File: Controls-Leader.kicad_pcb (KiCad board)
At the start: 2 copper layers, 99.5 x 94.2 mm, 164 parts, among them J1 Left_Signal, J10 Conn_02x03_Top_Bottom, J11 Conn_02x03_Top_Bottom, J12 Conn_01x04, J13 Conn_01x04, J18 PowerConn, J2 Right_Signal, J20 MotorCANConnector, J21 CAN_IN, J22 CAN_OUT, J23 USB_B_Micro, J24 ExtraGPIO_Conn, J25 UART_TP, J26 CAN_TP, J27 CAN_TP, J28 KILL_SW_IND, J29 Headlight, J3 Brake Light, J30 Backup Camera, J4 Headlight, J5 MinionConn, J6 SPI, J7 BPS_PWR_OUT, J8 SWD, J9 POW_2ND_CONN, SW1 BACKUP_SW, SW10 RESET, SW8 SW_Rotary2x6, U1 EL3H7, U10 EL3H7, U11 EL3H7, U12 RI3-1205S, U13 NCP1117-3.3_SOT223, U14 ADM3055E, U15 CDSOT23-T24CAN, U17 ADM3055E, U18 CDSOT23-T24CAN, U19 CP2102N-A01-GQFN24, U2 EL3H7, U3 EL3H7, U4 EL3H7, U5 EL3H7, U6 EL3H7, U7 STM32F413RHTx, U8 EL3H7, U9 EL3H7, Y1 Crystal

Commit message: layout in progress
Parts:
- removed C18, C19: 0.1uF, Capacitor_SMD:C_0805_2012Metric
- removed C2, C3, C32: 1u, Capacitor_SMD:C_0805_2012Metric
- removed C20: 10u, UTSVT_Passive:C_2220_5750Metric
- removed D1: KILL_SW_LED, UTSVT_Connectors:Molex_MicroFit3.0_1x2xP3.00mm_PolarizingPeg_Vertical
- removed D4, D5: BAS70-04, Package_TO_SOT_SMD:SOT-23
- removed D6: TVS, Diode_SMD:D_SOD-323
- removed J13: Conn_01x04, Connector_Molex:Molex_Micro-Fit_3.0_43650-0415_1x04_P3.00mm_Vertical
- removed J20: MotorCANConnector, UTSVT_Connectors:TE_4-2172079-2
- removed J28: KILL_SW_IND, UTSVT_Connectors:Molex_MicroFit3.0_1x2xP3.00mm_PolarizingPeg_Vertical
- removed J29: Headlight, UTSVT_Connectors:Molex_MicroFit3.0_1x2xP3.00mm_PolarizingPeg_Vertical
- removed J30: Backup Camera, Connector_Molex:Molex_Micro-Fit_3.0_43650-0215_1x02_P3.00mm_Vertical
- removed JP3, JP4: Jumper_2_Bridged, Jumper:SolderJumper-2_P1.3mm_Open_Pad1.0x1.5mm
- removed L1, L2, L3, L4, L9: 22u, Inductor_SMD:L_0805_2012Metric
- removed PS1, PS2, PS3, PS4, PS5: RCD-24, UTSVT_Special:RCD-24
- removed SW1: BACKUP_SW, Connector_Molex:Molex_Micro-Fit_3.0_43650-0315_1x03_P3.00mm_Vertical
- removed SW8: SW_Rotary2x6, Connector_Molex:Molex_Micro-Fit_3.0_43045-1412_2x07_P3.00mm_Vertical
- removed TP1: LEFT_BLINK, TestPoint:TestPoint_Pad_D1.5mm
- removed TP13: +12VA_TP, TestPoint:TestPoint_Pad_1.5x1.5mm
- removed TP14: GND1_TP, TestPoint:TestPoint_Pad_1.5x1.5mm
- removed TP2: +12V_TP, TestPoint:TestPoint_Pad_1.5x1.5mm
- removed TP3: GNDPWR_TP, TestPoint:TestPoint_Pad_1.5x1.5mm
- removed U10, U11: EL3H7, Package_SO:SOP-4_4.4x2.6mm_P1.27mm
- added BRAKELIGHT1: EXTERNAL_BRAKELIGHT, Connector_Molex:Molex_Micro-Fit_3.0_43650-0215_1x02_P3.00mm_Vertical, F.Cu at (125.5, 168.3)
- added D10: Motor Controller Fault, LED_SMD:LED_0805_2012Metric, F.Cu at (30.0, 37.3)
- added D11: Ignition 1, LED_SMD:LED_0805_2012Metric, F.Cu at (30.0, 40.3)
- added D12: Ignition 2, LED_SMD:LED_0805_2012Metric, F.Cu at (30.0, 43.4)
- added D13: BPS Fault, LED_SMD:LED_0805_2012Metric, F.Cu at (30.0, 46.4)
- added D16: Control Fault, LED_SMD:LED_0805_2012Metric, F.Cu at (30.0, 49.5)
- added D17: SD12_SOD323, Diode_SMD:D_SOD-323, F.Cu at (110.3, 7.05)
- added D18: A_CNCTR, LED_SMD:LED_0805_2012Metric, F.Cu at (30.0, 52.5)
- added D7: M_CNCTR, LED_SMD:LED_0805_2012Metric, F.Cu at (30.0, 31.2)
- added D9: OS Error, LED_SMD:LED_0805_2012Metric, F.Cu at (30.0, 34.3)
- added F1: Fuse, Fuse:Fuse_1206_3216Metric, F.Cu at (109.4, 57.3)
- added J14: Conn_02x04_Odd_Even, UTSVT_Connectors:Molex_MicroFit3.0_2x4xP3.00mm_PolarizingPeg_Vertical, F.Cu at (221.0, 82.2)
- added LOGO3: Dr. Hallock Logo, UTSVT_Special:Hallock_Image_Small, F.Cu at (7.62, -15.2)
- added LOGO4: UTSVT Logo, UTSVT_Special:UTSVT_Logo_Symbol, F.Cu at (-5.08, 7.62)
- added L_BLINK_EXT1: EXTERNAL_LEFTBLINK, Connector_Molex:Molex_Micro-Fit_3.0_43650-0215_1x02_P3.00mm_Vertical, F.Cu at (112.2, 168.3)
- added Q1: IRLML0030, Package_TO_SOT_SMD:SOT-23, F.Cu at (113.8, 161.0)
- added Q2: IRLML0030, Package_TO_SOT_SMD:SOT-23, F.Cu at (111.3, 21.7)
- added Q3: IRLML0030, Package_TO_SOT_SMD:SOT-23, F.Cu at (100.3, 161.0)
- added Q4: IRLML0030, Package_TO_SOT_SMD:SOT-23, F.Cu at (85.8, 79.1)
- added Q5: IRLML0030, Package_TO_SOT_SMD:SOT-23, F.Cu at (30.4, 79.7)
- added Q6: IRLML0030, Package_TO_SOT_SMD:SOT-23, F.Cu at (30.4, 84.4)
- added R28: 698, Resistor_SMD:R_0805_2012Metric, F.Cu at (19.4, 44.4)
- added R31: 698, Resistor_SMD:R_0805_2012Metric, F.Cu at (19.4, 47.3)
- added R33: 4.9k, Resistor_SMD:R_0805_2012Metric, F.Cu at (17.0, 78.8)
- added R39: 2k, Resistor_SMD:R_0805_2012Metric, F.Cu at (17.0, 81.8)
- added R41: 100k, Resistor_SMD:R_0805_2012Metric, F.Cu at (81.1, 77.8)
- added R50: 4.9k, Resistor_SMD:R_0805_2012Metric, F.Cu at (17.0, 84.7)
- added R52: 2k, Resistor_SMD:R_0805_2012Metric, F.Cu at (17.0, 87.7)
- added R53: 4.9k, Resistor_SMD:R_0805_2012Metric, F.Cu at (21.4, 78.8)
- added R55: 2k, Resistor_SMD:R_0805_2012Metric, F.Cu at (21.4, 81.8)
- added R56: 100k, Resistor_SMD:R_0805_2012Metric, F.Cu at (81.1, 80.7)
- added R58: 100k, Resistor_SMD:R_0805_2012Metric, F.Cu at (81.1, 83.7)
- added R59: 4.9k, Resistor_SMD:R_0805_2012Metric, F.Cu at (21.4, 84.7)
- added R60: 2k, Resistor_SMD:R_0805_2012Metric, F.Cu at (21.4, 87.7)
- added R61: 4.9k, Resistor_SMD:R_0805_2012Metric, F.Cu at (25.8, 78.8)
- added R62: 2k, Resistor_SMD:R_0805_2012Metric, F.Cu at (25.8, 81.8)
- added R63: 4.9k, Resistor_SMD:R_0805_2012Metric, F.Cu at (25.8, 84.7)
- added R64: 2k, Resistor_SMD:R_0805_2012Metric, F.Cu at (25.8, 87.7)
- added R8: 698, Resistor_SMD:R_0805_2012Metric, F.Cu at (15.0, 44.4)
- added R9: 698, Resistor_SMD:R_0805_2012Metric, F.Cu at (15.0, 47.3)
- added R_BLINK_EXT1: EXTERNAL_RIGHTBLINK, Connector_Molex:Molex_Micro-Fit_3.0_43650-0215_1x02_P3.00mm_Vertical, F.Cu at (98.6, 168.3)
- added U23: EL3H7, Package_DIP:DIP-4_W7.62mm, F.Cu at (1.12, 80.9)
- added U24: EL3H7, Package_DIP:DIP-4_W7.62mm, F.Cu at (1.12, 87.6)
- added U25: EL3H7, Package_DIP:DIP-4_W7.62mm, F.Cu at (69.7, 76.2)
- added U26: EL3H7, Package_DIP:DIP-4_W7.62mm, F.Cu at (101.6, 148.6)
- added U27: EL3H7, Package_DIP:DIP-4_W7.62mm, F.Cu at (1.12, 94.3)
- added U28: EL3H7, Package_DIP:DIP-4_W7.62mm, F.Cu at (1.12, 101.0)
- added U29: EL3H7, Package_DIP:DIP-4_W7.62mm, F.Cu at (16.5, 116.8)
- C1: value 1u -> 1uF
- C14, C15, C28, C38, C41, LOGO1: moved to F.Cu
- C4: value 1u -> 10u
- J1: value Left_Signal -> Conn_01x02; footprint UTSVT_Connectors:Molex_MicroFit3.0_1x2xP3.00mm_PolarizingPeg_Vertical -> Connector_Molex:Molex_Micro-Fit_3.0_43650-0215_1x02_P3.00mm_Vertical
- J10, J11: value Conn_02x03_Top_Bottom -> Conn_01x02; footprint Connector_Molex:Molex_Micro-Fit_3.0_43045-0612_2x03_P3.00mm_Vertical -> Connector_Molex:Molex_Micro-Fit_3.0_43650-0215_1x02_P3.00mm_Vertical
- J12: value Conn_01x04 -> Conn_01x02; footprint Connector_Molex:Molex_Micro-Fit_3.0_43650-0415_1x04_P3.00mm_Vertical -> Connector_Molex:Molex_Micro-Fit_3.0_43650-0215_1x02_P3.00mm_Vertical
- J2: value Right_Signal -> UART_TP; footprint UTSVT_Connectors:Molex_MicroFit3.0_1x2xP3.00mm_PolarizingPeg_Vertical -> Connector_PinHeader_2.54mm:PinHeader_1x03_P2.54mm_Vertical
- J3: value Brake Light -> ExtraGPIO_Conn; footprint UTSVT_Connectors:Molex_MicroFit3.0_1x2xP3.00mm_PolarizingPeg_Vertical -> Connector_PinHeader_2.54mm:PinHeader_2x05_P2.54mm_Vertical
- J4: value Headlight -> Conn_02x05_Top_Bottom; footprint UTSVT_Connectors:Molex_MicroFit3.0_1x2xP3.00mm_PolarizingPeg_Vertical -> UTSVT_Connectors:Molex_MicroFit3.0_2x6xP3.00mm_PolarizingPeg_Vertical
- J5: value MinionConn -> M_CAN_IN; footprint Connector_Molex:Molex_Micro-Fit_3.0_43045-1012_2x05_P3.00mm_Vertical -> Connector_Molex:Molex_Micro-Fit_3.0_43045-0612_2x03_P3.00mm_Vertical
- J6: value SPI -> Conn_01x04; footprint Connector_PinHeader_2.54mm:PinHeader_1x04_P2.54mm_Vertical -> Connector_Molex:Molex_Micro-Fit_3.0_43650-0415_1x04_P3.00mm_Vertical
- J7: value BPS_PWR_OUT -> Conn_01x03; footprint UTSVT_Connectors:Molex_MicroFit3.0_1x2xP3.00mm_PolarizingPeg_Vertical -> Connector_Molex:Molex_Micro-Fit_3.0_43650-0315_1x03_P3.00mm_Vertical
- J9: value POW_2ND_CONN -> Conn_01x03; footprint UTSVT_Connectors:Molex_MicroFit3.0_1x2xP3.00mm_PolarizingPeg_Vertical -> Connector_Molex:Molex_Micro-Fit_3.0_43650-0315_1x03_P3.00mm_Vertical
- L5, L6, L7, L8: value 2kH -> https://www.mouser.com/ProductDetail/963-BK2125LM182-T
- R1, R2, R3, R4: value 105 -> 698
- R10: value 4.9k -> 2k
- R11: value 4.9k -> 510
- R12: value 1.2k -> 510
- R19: value 5.1k -> 510
- R20: value 5.1k -> 100k
- R22: value 10k -> 510
- R23: value 10k -> 100k
- R26, R27: value 105R -> 10k
- R5: value 510 -> 2k
- R7: value 1.5k -> 5.1k
- TP10: value POWER -> GND_UNISO; footprint TestPoint:TestPoint_Pad_1.5x1.5mm -> TestPoint:TestPoint_Keystone_5005-5009_Compact
- TP7: footprint TestPoint:TestPoint_Pad_D1.5mm -> TestPoint:TestPoint_Pad_1.5x1.5mm
- TP8: value BK_LIGHT -> LEFT_BLINK; footprint TestPoint:TestPoint_Pad_D1.5mm -> TestPoint:TestPoint_Pad_1.5x1.5mm
- TP9: value Headlight_PWR -> 12V_UNISO; footprint TestPoint:TestPoint_Pad_D1.5mm -> TestPoint:TestPoint_Keystone_5005-5009_Compact
- U1, U2, U3, U4, U5, U6, U8, U9: footprint Package_SO:SOP-4_4.4x2.6mm_P1.27mm -> Package_DIP:DIP-4_W7.62mm
- moved LOGO1 166.5 mm to (-40.6, 22.9), turned to 0 degrees
- moved U4 165.6 mm to (1.12, 67.5), turned to 0 degrees
- moved H4 163.7 mm to (53.3, 170.2), turned to 0 degrees
- moved U2 160.6 mm to (1.12, 60.8), turned to 0 degrees
- moved R4 158.1 mm to (15.0, 41.4), turned to 0 degrees
- moved R3 152.4 mm to (10.6, 47.3), turned to 0 degrees
- moved R2 150.6 mm to (10.6, 44.4), turned to 0 degrees
- moved U5 150.0 mm to (1.12, 74.2), turned to 0 degrees
- moved J22 149.8 mm to (244.4, 124.0), turned to 0 degrees
- moved R1 149.3 mm to (10.6, 41.4), turned to 0 degrees
- moved J1 147.8 mm to (43.7, 44.0), turned to 0 degrees
- moved J21 147.4 mm to (244.4, 116.8), turned to 0 degrees
- moved H3 136.6 mm to (228.6, 172.7)
- moved LOGO2 133.4 mm to (-5.08, 15.2)
- moved U12 131.0 mm to (97.2, 6.60), turned to 0 degrees
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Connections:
- C1 pad 1: GNDPWR -> /Brake_SW
- C1 pad 2: +12V -> GND
- C4 pad 1: GNDPWR -> +12V
- C4 pad 2: +12V -> Net-(Q2-D)
- J1 pad 1: Net-(J1-Pad1) -> /ADC1_IN8
- J1 pad 2: Net-(J1-Pad2) -> /ADC1_IN9
- J10 pad 1: +3V3 -> Net-(J10-Pin_1)
- J10 pad 2: Net-(R15-Pad1) -> Net-(J10-Pin_2)
- J11 pad 1: +3V3 -> Net-(J11-Pin_1)
- J11 pad 2: Net-(R16-Pad1) -> Net-(J11-Pin_2)
- J12 pad 1: Net-(U9-Pad4) -> +3.3V
- J12 pad 2: Net-(U9-Pad3) -> Net-(J12-Pin_2)
- J2 pad 1: Net-(J2-Pad1) -> GND
- J2 pad 2: Net-(J2-Pad2) -> /UART4_Tx
- J24 pad 2: /PB4 -> /PB2
- J24 pad 4: /PB5 -> /PB3
- J24 pad 6: /PB6 -> /PD2
- J24 pad 8: /PB7 -> /PC12
- J3 pad 1: Net-(J3-Pad1) -> /PC8
- J3 pad 2: Net-(J3-Pad2) -> /PC2
- J4 pad 1: Net-(J4-Pad1) -> +12V
- J4 pad 2: Net-(J4-Pad2) -> /DashAndDisplay/BPS_Hzd
- J5 pad 1: +5V -> Net-(J5-Pin_1)
- J5 pad 3: /MOSI -> unconnected-(J5-Pin_3-Pad3)
- J5 pad 4: /MISO -> /Motor_CAN/CAN_H
- J5 pad 5: /BPS_PWR -> /Motor_CAN/CAN_L
- J5 pad 6: /UART3_Tx -> unconnected-(J5-Pin_6-Pad6)
- J6 pad 1: /MOSI -> +5V
- J6 pad 2: /MISO -> GND
- J6 pad 3: /CLK -> /UART3_Tx
- J6 pad 4: /CS -> /UART3_Rx
- J7 pad 1: /BPS_PWR -> +3V3
- J7 pad 2: GNDPWR -> Net-(J7-Pin_2)
- J9 pad 1: Net-(J9-Pad1) -> +3V3
- J9 pad 2: GNDPWR -> Net-(J9-Pin_2)
- R1 pad 1: Net-(R1-Pad1) -> /Motor_PRCHG_Bypass
- R1 pad 2: /LEFT_BLINK -> Net-(D7-A)
- R10 pad 1: +3V3 -> Net-(R10-Pad1)
- R10 pad 2: /IG1 -> /Left_Ind
- R11 pad 1: +3V3 -> /Lights/RIGHT_BLINK
- R11 pad 2: /IG2 -> Net-(R11-Pad2)
- R12 pad 1: Net-(J28-Pad1) -> /Lights/LEFT_BLINK
- R15 pad 1: Net-(R15-Pad1) -> Net-(J7-Pin_2)
- R16 pad 1: Net-(R16-Pad1) -> Net-(J9-Pin_2)
- R19 pad 1: +3V3 -> /Heartbeat
- R19 pad 2: /Brake_Pot2 -> Net-(R19-Pad2)
- R2 pad 1: Net-(R2-Pad1) -> /OS_Fault
- R2 pad 2: /RIGHT_BLINK -> Net-(D9-A)
- R20 pad 1: /Accel_Pot2 -> Net-(Q5-G)
- R20 pad 2: GND -> GNDPWR
- R22 pad 1: Net-(R22-Pad1) -> /Bps_Hazard
- R22 pad 2: /Accel_Pot2 -> Net-(R22-Pad2)
- R23 pad 1: Net-(R23-Pad1) -> Net-(Q6-G)
- R23 pad 2: /Brake_Pot2 -> GNDPWR
- R24 pad 2: /M_PRCHG -> /Array_PRCHG_Bypass
- R25 pad 2: /M_CNCTR -> /Motor_PRCHG_Bypass
- R26 pad 1: Net-(R26-Pad1) -> Net-(J12-Pin_2)
- R26 pad 2: /A_CNCTR -> GND
- R27 pad 1: Net-(R27-Pad1) -> /Brake_SW
- R27 pad 2: /A_PRCHG -> Net-(J12-Pin_2)
- R3 pad 1: Net-(R3-Pad1) -> /Motor_Controller_Fault
- R3 pad 2: /BK_LIGHT -> Net-(D10-A)
- R4 pad 1: Net-(R4-Pad1) -> /IG1
- R4 pad 2: /Headlight_ON -> Net-(D11-A)
- R5 pad 2: Net-(R5-Pad2) -> /Right_Ind
- R6 pad 1: Net-(R6-Pad1) -> /Brake_Light
- TP10 pad 1: Net-(SW8-Pad11) -> GNDPWR
- TP7 pad 1: /RIGHT_BLINK -> /Lights/RIGHT_BLINK
- TP8 pad 1: /BK_LIGHT -> /Lights/LEFT_BLINK
- TP9 pad 1: /Headlight_ON -> +12V
- U1 pad 1: Net-(R1-Pad1) -> Net-(R10-Pad1)
- U1 pad 2: GND -> GNDPWR
- U1 pad 3: Net-(PS1-Pad3) -> /Lights/LEFT_BLINK
- U1 pad 4: +12V -> /TimerCLK
- U12 pad 1: GNDPWR -> Net-(Q2-D)
- U2 pad 1: Net-(R2-Pad1) -> Net-(R39-Pad2)
- U2 pad 2: GND -> GNDPWR
- U2 pad 3: Net-(PS2-Pad3) -> /IG1
- U2 pad 4: +12V -> +3V3
- U3 pad 1: Net-(R3-Pad1) -> Net-(R6-Pad2)
- U4 pad 1: Net-(R4-Pad1) -> Net-(R19-Pad2)
- U4 pad 3: Net-(PS4-Pad3) -> Net-(Q5-G)
- U5 pad 1: Net-(R5-Pad2) -> Net-(R22-Pad2)
- U5 pad 2: GNDPWR -> GND
- U5 pad 3: GND -> Net-(Q6-G)
- U5 pad 4: /IG1 -> +12V
- U6 pad 1: Net-(R6-Pad2) -> Net-(R5-Pad1)
- U6 pad 3: GND -> /Lights/RIGHT_BLINK
- U6 pad 4: /IG2 -> /TimerCLK
- U7 pad 10: /Accel_Pot2 -> /PC2
- U7 pad 11: /Brake_Pot2 -> /PC3
- U7 pad 20: /CS -> /Bps_Hazard
- U7 pad 21: /CLK -> /Forward
- U7 pad 22: /MISO -> /Reverse
- U7 pad 23: /MOSI -> /Cruise_En
- U7 pad 24: unconnected-(U7-Pad24) -> /PC4
- U7 pad 26: unconnected-(U7-Pad26) -> /ADC1_IN8
- U7 pad 27: unconnected-(U7-Pad27) -> /ADC1_IN9
- U7 pad 28: unconnected-(U7-Pad28) -> /PB2
- U7 pad 33: unconnected-(U7-Pad33) -> /UART4_Rx
- U7 pad 34: unconnected-(U7-Pad34) -> /UART4_Tx
- U7 pad 35: unconnected-(U7-Pad35) -> /BPS_Fault
- U7 pad 36: unconnected-(U7-Pad36) -> /Controls_Fault
- U7 pad 37: /Headlight_ON -> /PC6
- U7 pad 38: /BK_LIGHT -> /PC7
- U7 pad 39: /RIGHT_BLINK -> /PC8
- U7 pad 40: /LEFT_BLINK -> /Brake_SW
- U7 pad 42: unconnected-(U7-Pad42) -> /PA9
- U7 pad 43: unconnected-(U7-Pad43) -> /PA10
- U7 pad 51: /A_PRCHG -> /Array_PRCHG_Bypass
- U7 pad 52: /A_CNCTR -> /Motor_PRCHG_Bypass
- U7 pad 53: /M_CNCTR -> /PC12
- U7 pad 54: /M_PRCHG -> /PD2
- U7 pad 55: unconnected-(U7-Pad55) -> /PB3
- U7 pad 56: /PB4 -> /Cruise_Set
- U7 pad 57: /PB5 -> /Brake_Light
- U7 pad 58: /PB6 -> /Heartbeat
- U7 pad 59: /PB7 -> /TimerCLK
- U7 pad 61: unconnected-(U7-Pad61) -> /OS_Fault
- U7 pad 62: unconnected-(U7-Pad62) -> /Motor_Controller_Fault
- U8 pad 3: Net-(U8-Pad3) -> Net-(J10-Pin_2)
- U8 pad 4: Net-(U8-Pad4) -> Net-(J10-Pin_1)
- U9 pad 3: Net-(U9-Pad3) -> Net-(J11-Pin_2)
- U9 pad 4: Net-(U9-Pad4) -> Net-(J11-Pin_1)
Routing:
- net +3V3: track 299.6 -> 0.00 mm, vias 18 -> 0
- net +12V: track 190.8 -> 0.00 mm, vias 5 -> 0
- net GNDPWR: track 185.9 -> 0.00 mm, vias 43 -> 0
- net +5V: track 146.2 -> 0.00 mm, vias 6 -> 0
- net GND: track 71.2 -> 0.00 mm, vias 131 -> 0
- net /Accel_Pot: track 66.0 -> 0.00 mm
- net /Accel_Pot2: track 60.7 -> 0.00 mm
- net /Brake_Pot2: track 60.3 -> 0.00 mm, vias 4 -> 0
- net /Car_CAN/CAN_L: track 56.7 -> 0.00 mm, vias 1 -> 0
- net Net-(U15-GND): track 55.4 -> 0.00 mm, vias 4 -> 0
- net Net-(J21-Pin_2): track 54.2 -> 0.00 mm, vias 2 -> 0
- net /LEFT_BLINK: track 54.1 -> 0.00 mm
- net /UART3_Tx: track 53.9 -> 0.00 mm
- net /Car_CAN/CAN_H: track 53.5 -> 0.00 mm
- net /Brake_Pot: track 49.8 -> 0.00 mm, vias 2 -> 0
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- removed copper zone on B.Cu, net GND
- removed copper zone on F.Cu, net GND
- removed copper zone on B.Cu, net GNDPWR
- removed copper zone on F.Cu, net GNDPWR
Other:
- board outline removed
- board text removed: "+"
- board text removed: "+12V"
- board text removed: "+5V"
- board text removed: "-"
- board text removed: "12VA"
- board text removed: "3.3V"
- board text removed: "3V3"
- board text removed: "5V"
- board text removed: "Accel"
- board text removed: "Accel Cntctr"
- board text removed: "BPS Pwr"
- board text removed: "BPSEN"
- board text removed: "Backup Cam"
- board text removed: "Brake"
- board text removed: "CAN"
- board text removed: "CLK"
- board text removed: "CS"
- board text removed: "Camera Switch"
- board text removed: "Controls Leader Board v2.4 Chase Block & Hannah Lee April 2022"
- board text removed: "DIO"
- board text removed: "GND"
- board text removed: "GND1"
- board text removed: "GNDPWR"
- board text removed: "HeadLights"
- board text removed: "Headlight"
- board text removed: "Ign Sw"
- board text removed: "Kill Sw Ctrl"
- board text removed: "Kill Sw LED"
- board text removed: "Left"
- board text removed: "Left Blink"
- board text removed: "MISO"
- board text removed: "MOSI"
- board text removed: "Minion"
- board text removed: "Motor Cntctr"
- board text removed: "Pwr 2nd Conn"
- board text removed: "Right"
- board text removed: "Right Blink"
- board text removed: "Rx"
- board text removed: "TO-DOS: - Fix minion brd connector so that way 12v and gndpwr and 5v and gnd are next to each other respectively. It would also be nice to change it to be a larger connector so we can send +5v and gnd to the minion brd - Finish labelling the connector and test points in the power section - Finish the traces - Rename the board"
- board text removed: "Tx"

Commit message: routing done for optocouplers
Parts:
- moved U6 186.3 mm to (133.5, 186.6), turned to 90 degrees
- moved R5 182.6 mm to (134.1, 189.8), turned to 180 degrees
- moved U1 172.2 mm to (137.7, 163.6)
- moved TP7 169.8 mm to (150.6, 168.9)
- moved TP8 168.1 mm to (154.2, 168.9)
- moved U2 163.9 mm to (116.3, 177.3), turned to 90 degrees
- moved U4 162.6 mm to (137.2, 156.5)
- moved R4 158.6 mm to (117.5, 162.6), turned to 180 degrees
- moved R10 157.3 mm to (134.5, 166.1), turned to -90 degrees
- moved R20 156.0 mm to (148.8, 157.6), turned to -90 degrees
- moved U24 152.9 mm to (125.0, 177.3), turned to 90 degrees
- moved R8 148.5 mm to (105.0, 162.6), turned to 180 degrees
- moved D11 147.4 mm to (117.4, 159.0), turned to 180 degrees
- moved R19 145.2 mm to (134.4, 157.8), turned to -90 degrees
- moved U23 144.5 mm to (108.7, 177.3), turned to 90 degrees
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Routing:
- net Net-(Q5-G): track 0.00 -> 37.1 mm
- net Net-(Q6-G): track 0.00 -> 32.1 mm
- net /Left_Ind: track 0.00 -> 25.7 mm
- net /Lights/RIGHT_BLINK: track 0.00 -> 22.0 mm
- net /DashAndDisplay/IGN_2_Motor: track 0.00 -> 21.2 mm
- net /Lights/LEFT_BLINK: track 0.00 -> 18.4 mm
- net Net-(R11-Pad2): track 0.00 -> 18.2 mm
- net Net-(R62-Pad2): track 0.00 -> 17.0 mm
- net Net-(J10-Pin_1): track 0.00 -> 15.2 mm
- net Net-(J11-Pin_1): track 0.00 -> 15.1 mm
- net Net-(J11-Pin_2): track 0.00 -> 14.8 mm
- net Net-(J10-Pin_2): track 0.00 -> 14.8 mm
- net Net-(R60-Pad2): track 0.00 -> 13.9 mm
- net Net-(R24-Pad1): track 0.00 -> 12.9 mm
- net Net-(R25-Pad1): track 0.00 -> 12.9 mm
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
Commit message: layout done except connecting uc to everything and vias for power and gnd plane
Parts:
- D10: value Motor Controller Fault -> Motor Fault
- moved J6 204.0 mm to (81.7, 58.5), turned to -90 degrees
- moved J1 186.1 mm to (212.8, 122.0), turned to 90 degrees
- moved R3 165.8 mm to (165.0, 107.7)
- moved R9 155.1 mm to (158.9, 105.2)
- moved D10 151.1 mm to (165.0, 105.2), turned to 180 degrees
- moved J14 148.1 mm to (80.7, 129.9)
- moved C4 143.6 mm to (208.7, 101.3), turned to 90 degrees
- moved D13 142.7 mm to (158.8, 107.7)
- moved TP9 142.2 mm to (209.2, 109.3)
- moved R28 141.5 mm to (147.2, 105.2)
- moved U12 141.4 mm to (203.6, 99.7), turned to 90 degrees
- moved R2 139.4 mm to (136.1, 105.2)
- moved C40 137.9 mm to (196.0, 53.2), turned to -90 degrees
- moved R18 136.1 mm to (151.4, 74.8)
- moved C39 135.1 mm to (193.0, 53.2), turned to -90 degrees
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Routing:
- net Net-(J21-Pin_2): track 0.00 -> 86.4 mm
- net /Car_CAN/CAN_H: track 0.00 -> 82.7 mm
- net /UART3_Rx: track 0.00 -> 77.3 mm
- net /Motor_CAN/CAN_H: track 0.00 -> 73.2 mm
- net /UART3_Tx: track 0.00 -> 71.3 mm
- net /Accel_Pot: track 0.00 -> 61.9 mm
- net /Car_CAN/CAN_L: track 0.00 -> 60.7 mm
- net Net-(J21-Pin_1): track 0.00 -> 57.2 mm
- net /Motor_CAN/CAN_L: track 0.00 -> 49.6 mm
- net /Brake_Pot: track 0.00 -> 40.7 mm
- net Net-(U15-GND): track 0.00 -> 27.2 mm
- net /Brake_SW: track 0.00 -> 26.9 mm
- net /NRST: track 0.00 -> 20.6 mm
- net Net-(C37-Pad2): track 0.00 -> 13.7 mm
- net +5V: track 0.00 -> 12.6 mm
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- added copper zone on In1.Cu, net +3.3V
- added copper zone on In2.Cu, net GND
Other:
- board outline added: 137.7 x 115.3 mm
- copper layers 2 -> 4

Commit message: Shuffled some things closer together.
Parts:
- moved J1 45.8 mm to (196.3, 79.2)
- moved C16 23.1 mm to (109.1, 64.5)
- moved C17 23.1 mm to (109.1, 79.8)
- moved D2 23.1 mm to (109.5, 68.5)
- moved R13 23.1 mm to (105.5, 83.9)
- moved R14 23.1 mm to (105.5, 68.5)
- moved R15 23.1 mm to (105.5, 64.5)
- moved R16 23.1 mm to (105.5, 79.8)
- moved R26 23.1 mm to (109.4, 96.1)
- moved C1 23.1 mm to (108.0, 92.5)
- moved D3 23.1 mm to (110.0, 83.9)
- moved J12 23.1 mm to (99.9, 94.0)
- moved J14 23.1 mm to (98.9, 115.8)
- moved J6 23.1 mm to (99.9, 44.4)
- moved J7 23.1 mm to (99.9, 62.5)
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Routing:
- net GND: track 0.00 -> 13.2 mm
- net Net-(J11-Pin_2): track 14.8 -> 1.59 mm
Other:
- board size 137.7 x 115.3 mm -> 137.7 x 115.6 mm

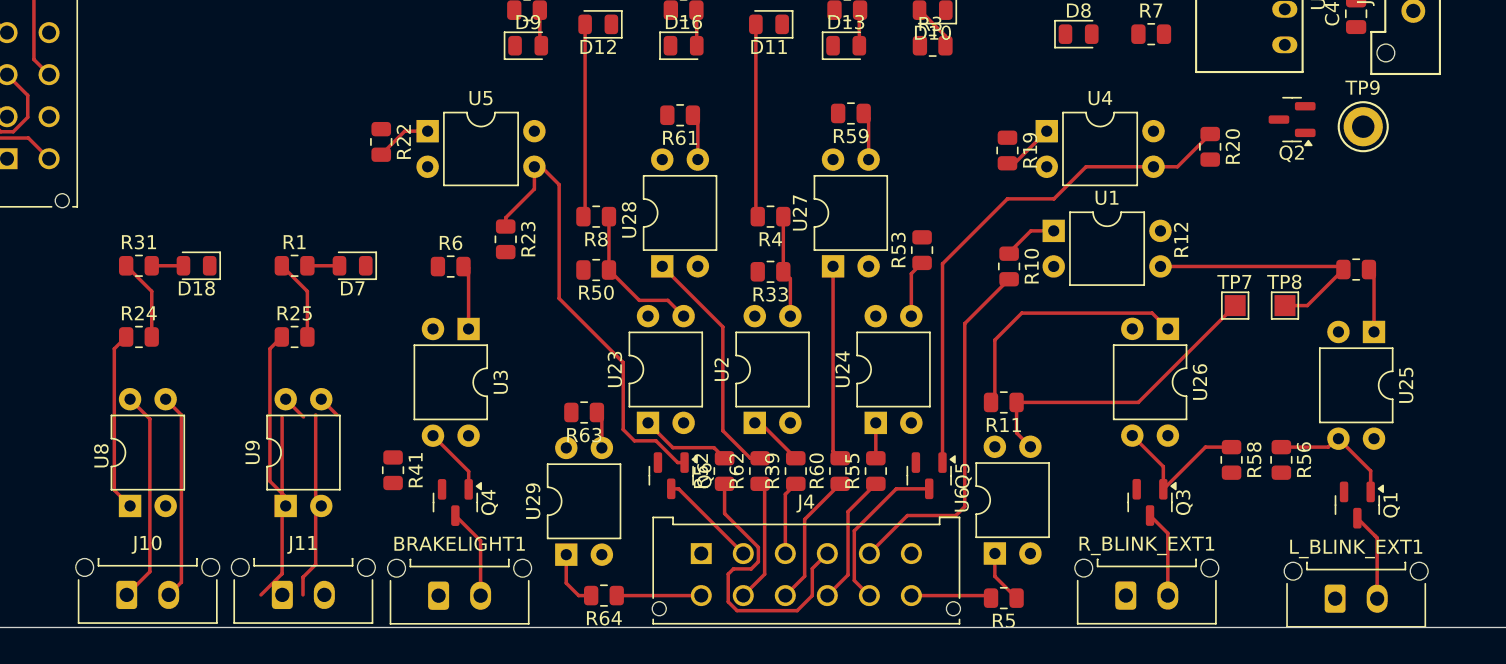
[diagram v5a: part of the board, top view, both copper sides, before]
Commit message: Changed EL3H7 footprint from through-hole to SMD.
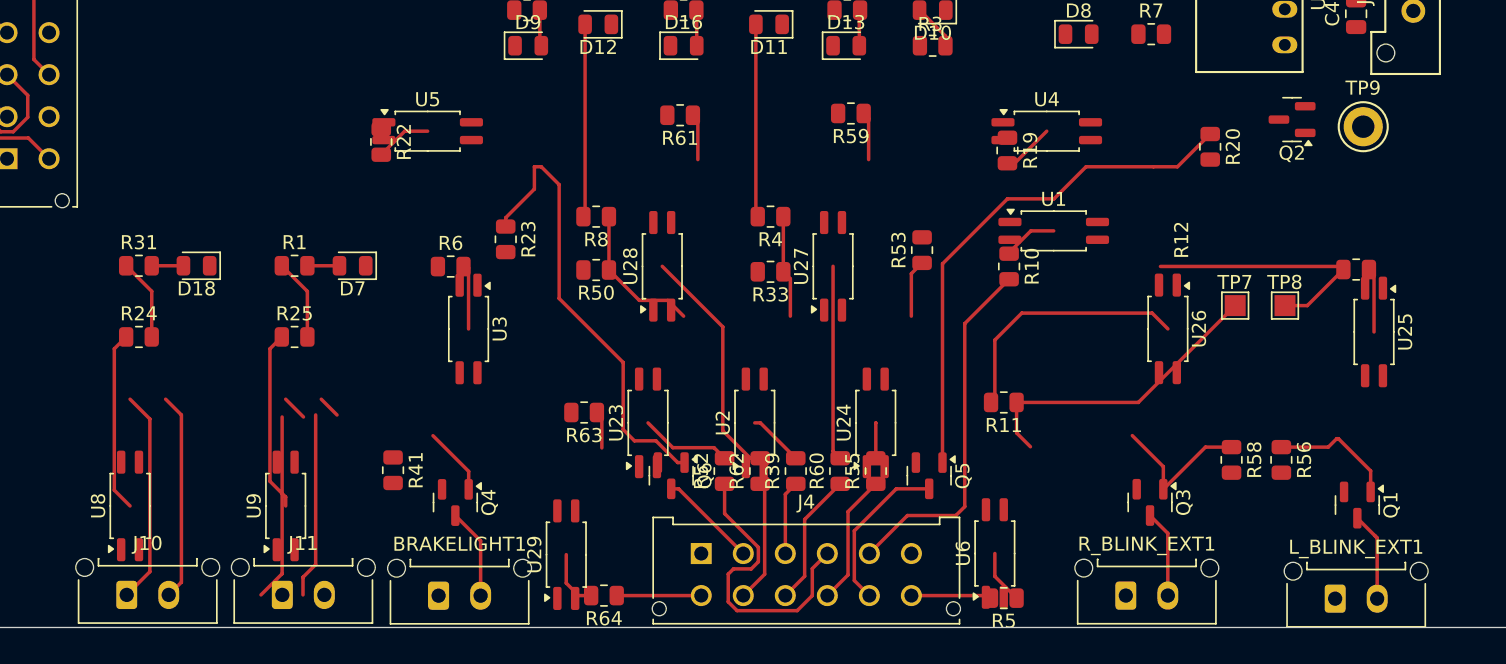
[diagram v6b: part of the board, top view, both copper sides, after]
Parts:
- D10: value Motor Fault -> Motor Controller Fault
- U1, U2, U23, U24, U25, U26, U27, U28, U29, U3, U4, U5, U6, U8, U9: footprint Package_DIP:DIP-4_W7.62mm -> Package_SO:SSOP-4_4.4x2.6mm_P1.27mm

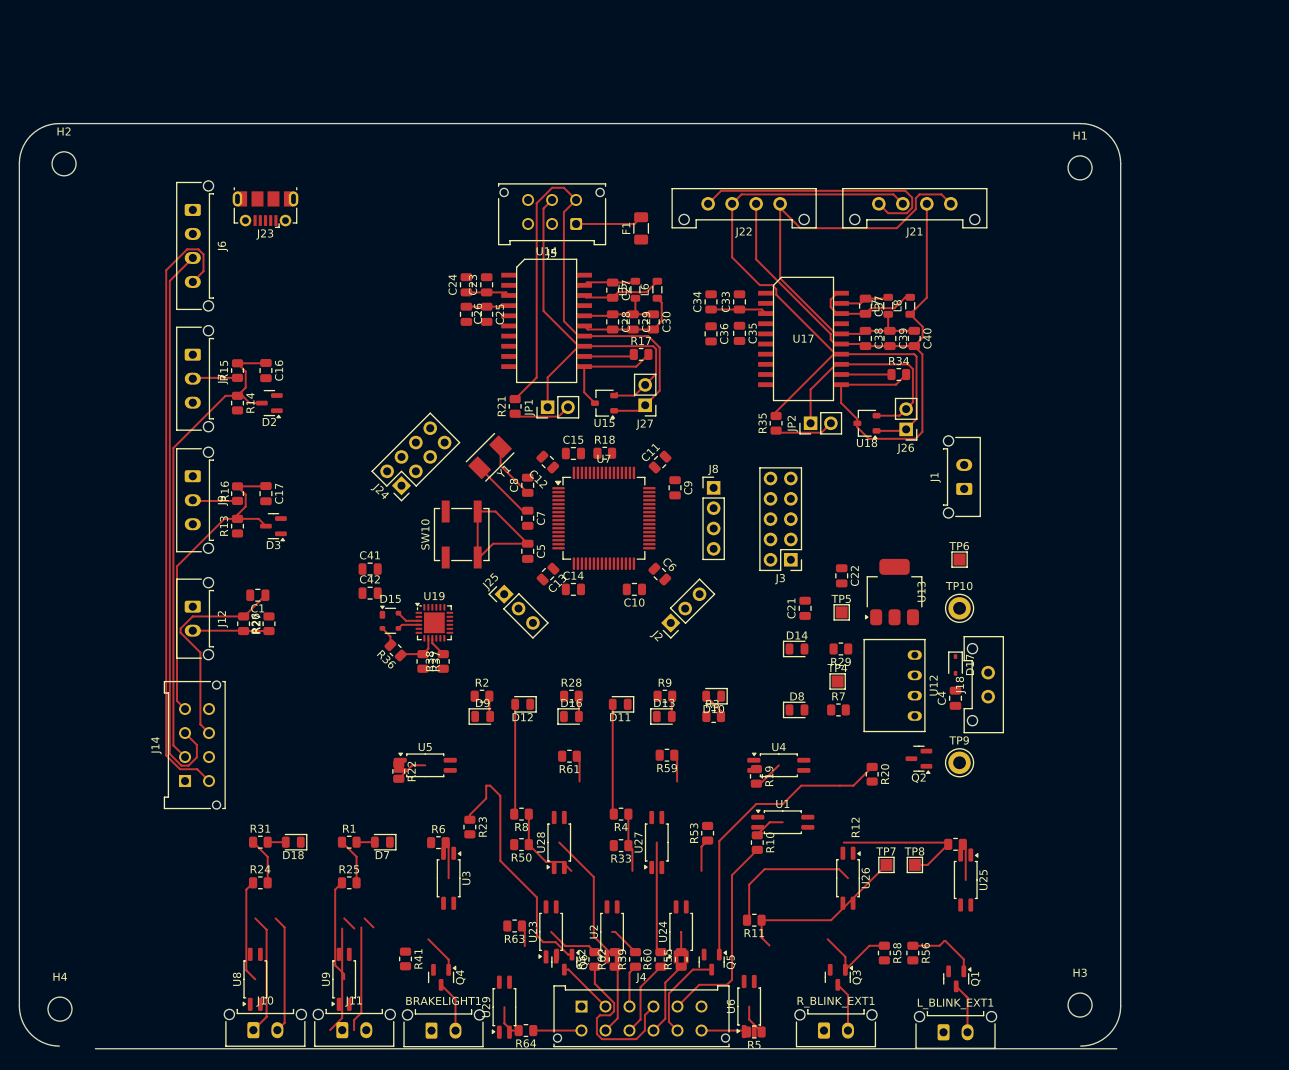
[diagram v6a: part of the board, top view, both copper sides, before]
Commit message: fixed routing for optoisolators (might need some spacing), made board a lil smaller, moved clock closer to mc, shuffled some stuff around
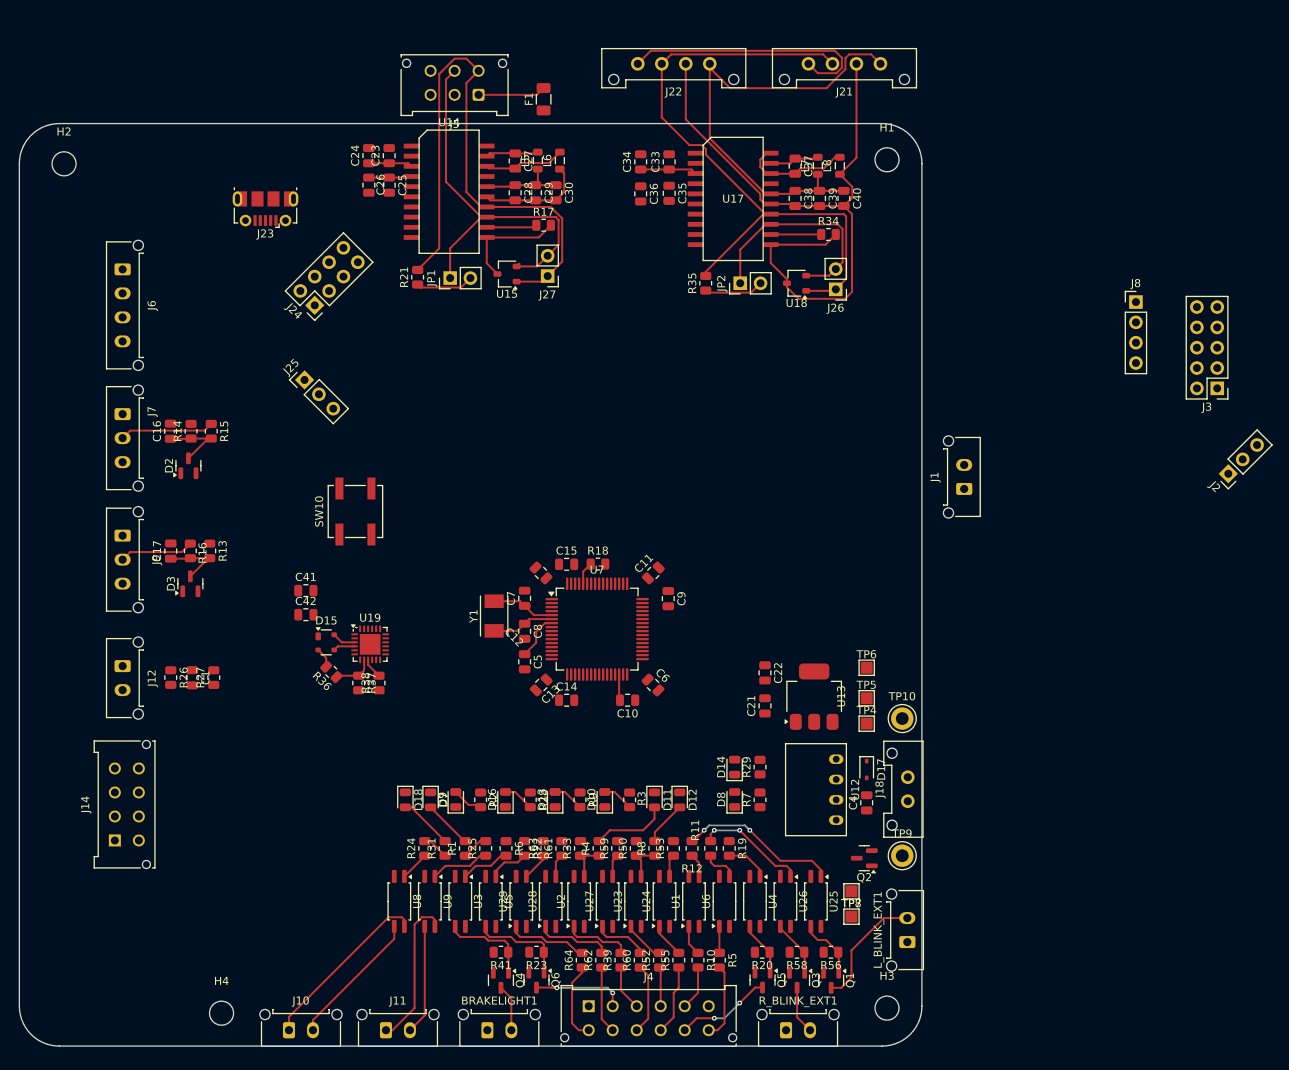
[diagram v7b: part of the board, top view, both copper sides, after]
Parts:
- moved J2 72.1 mm to (229.4, 77.4)
- moved J8 57.7 mm to (217.8, 55.9)
- moved J3 57.4 mm to (228.0, 66.7)
- moved J25 36.6 mm to (113.9, 65.6)
- moved R12 32.9 mm to (162.3, 124.2), turned to 90 degrees
- moved R20 26.1 mm to (171.1, 137.2), turned to 180 degrees
- moved J24 25.0 mm to (115.2, 56.3)
- moved H1 24.2 mm to (186.7, 38.1)
- moved H3 24.1 mm to (186.7, 144.1)
- moved R31 23.1 mm to (131.4, 124.2), turned to 90 degrees
- moved D12 23.0 mm to (160.8, 118.1), turned to -90 degrees
- moved R24 21.0 mm to (128.9, 124.2), turned to 90 degrees
- moved U8 20.5 mm to (125.7, 130.8), turned to -90 degrees
- moved J27 20.2 mm to (144.3, 52.6)
- moved R21 20.2 mm to (128.0, 52.8)
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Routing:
- net /UART3_Rx: track 77.3 -> 0.00 mm
- net /UART3_Tx: track 71.3 -> 0.00 mm
- net /Accel_Pot: track 61.9 -> 8.97 mm
- net /Brake_Pot: track 40.7 -> 8.26 mm
- net Net-(Q5-G): track 37.1 -> 6.82 mm
- net /Brake_SW: track 26.9 -> 0.00 mm
- net /Left_Ind: track 25.7 -> 5.53 mm
- net Net-(Q6-G): track 32.1 -> 12.2 mm
- net /Lights/RIGHT_BLINK: track 22.0 -> 4.39 mm
- net /DashAndDisplay/IGN_2_Motor: track 21.2 -> 4.91 mm
- net Net-(R12-Pad2): track 4.61 -> 20.1 mm, vias 0 -> 2
- net /Lights/LEFT_BLINK: track 18.4 -> 2.95 mm
- net /NRST: track 20.6 -> 5.78 mm
- net GND: track 13.2 -> 0.00 mm
- net Net-(J11-Pin_2): track 1.59 -> 13.7 mm
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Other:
- board size 137.7 x 115.6 mm -> 112.8 x 115.3 mm
